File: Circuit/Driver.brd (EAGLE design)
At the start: 160 x 100 mm, 1 part

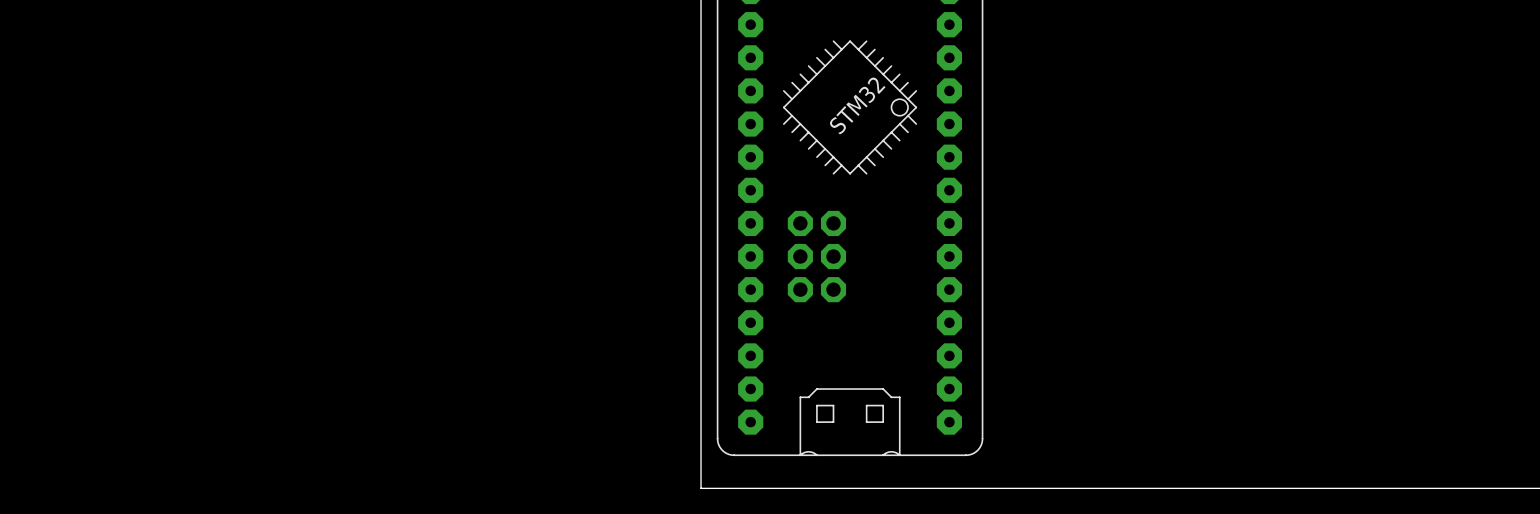
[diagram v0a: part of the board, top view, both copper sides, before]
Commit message: Add the mosfets and their driver to the BLDC Driver sch
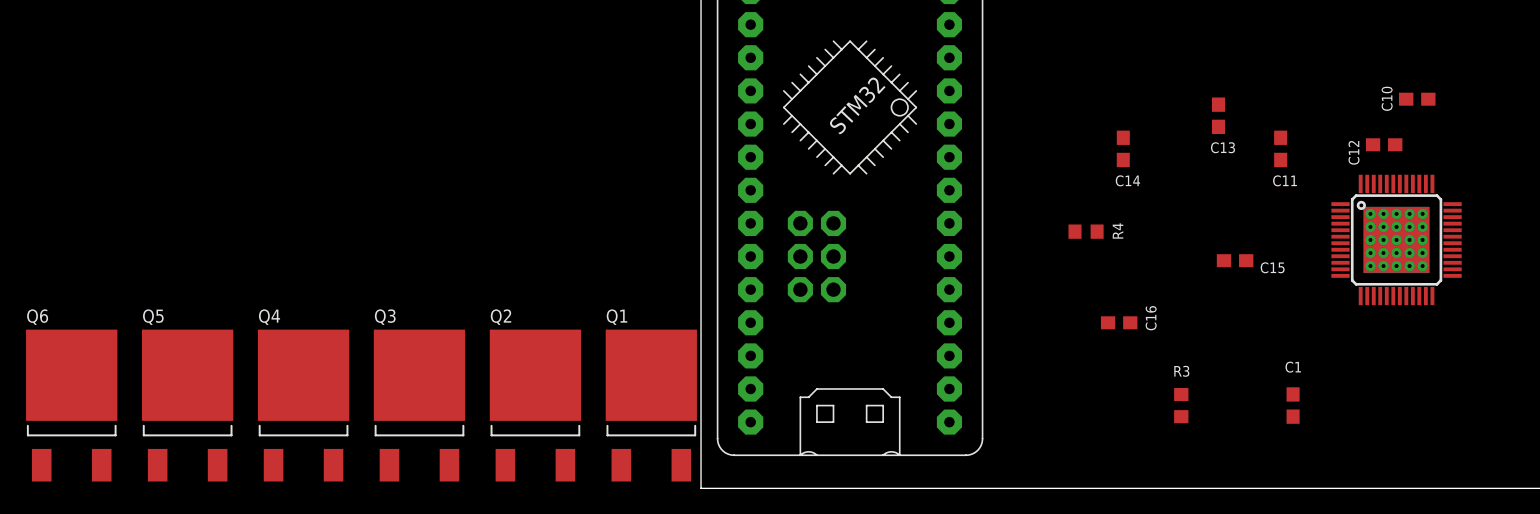
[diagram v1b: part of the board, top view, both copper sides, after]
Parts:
- added C1, C10, C15, C16: 1uF, rcl:C0603
- added C11: 2.2uF, rcl:C0603
- added C12: 4.7uF, rcl:C0603
- added C13, C14: 47nF, rcl:C0603
- added Q1, Q2, Q3, Q4, Q5, Q6: INFINEON_IRLR7843TRPBFINFINEON_IRLR7843TRPBF_0_0, IRLR7843:INFINEON_IRLR7843TRPBF_0
- added R3: 10k, rcl:R0603
- added R4: 100, rcl:R0603
- added U$3: DRV8305, BLDC project:PFB_S-PQFP-G48
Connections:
- net N$20 renamed VIN
- new net +5V: C16.1, R3.1, U$3.48
- new net A3: U$3.16
- new net A4: U$3.17
- new net A5: U$3.18
- new net D1: U$3.1
- new net D14: U$3.4
- new net D15: U$3.6
- new net D16: R3.2, U$3.13
- new net D17: U$3.9
- new net D18: U$3.10
- new net D19: U$3.11
- new net D20: U$3.12
- new net D8: U$3.2
- new net D9: U$3.8
- new net GH_A1: U$3.36
- new net GH_B1: U$3.29
- new net GH_C1: U$3.28
- new net GL_A1: U$3.33
- new net GL_B1: U$3.32
- new net GL_C1: U$3.25
- new net N$1: Q1.3, Q2.4
- new net N$15: C1.1, U$3.15
- new net N$16: C10.1, U$3.37
- new net N$17: C11.2, U$3.38
- new net N$18: C13.2, U$3.40
- new net N$19: C13.1, U$3.39
- new net N$2: Q3.3, Q4.4
- new net N$21: C14.2, U$3.43
- new net N$22: C14.1, U$3.42
- new net N$23: R4.1, U$3.44
- new net N$24: C15.1, U$3.46
- new net N$25: U$3.3
- new net N$26: U$3.5
- new net N$27: U$3.7
- new net N$5: Q5.3, Q6.4
- new net SH_A1: U$3.35
- new net SH_B1: U$3.30
- new net SH_C1: U$3.27
- new net SL_A1: U$3.23, U$3.34
- new net SL_B1: U$3.21, U$3.31
- new net SL_C1: U$3.19, U$3.26
- net GND: now also C1.2, C10.2, C12.2, C15.2, C16.2, U$3.14, U$3.20, U$3.22, U$3.24, U$3.45, U$3.P$1, U$3.P$10, U$3.P$11, U$3.P$12, U$3.P$13, U$3.P$14, U$3.P$15, U$3.P$16, U$3.P$17, U$3.P$18, U$3.P$19, U$3.P$2, U$3.P$20, U$3.P$21, U$3.P$22, U$3.P$23, U$3.P$24, U$3.P$25, U$3.P$26, U$3.P$27, U$3.P$3, U$3.P$4, U$3.P$5, U$3.P$6, U$3.P$7, U$3.P$8, U$3.P$9
- net VCC: now also C11.1, C12.1, R4.2, U$3.41

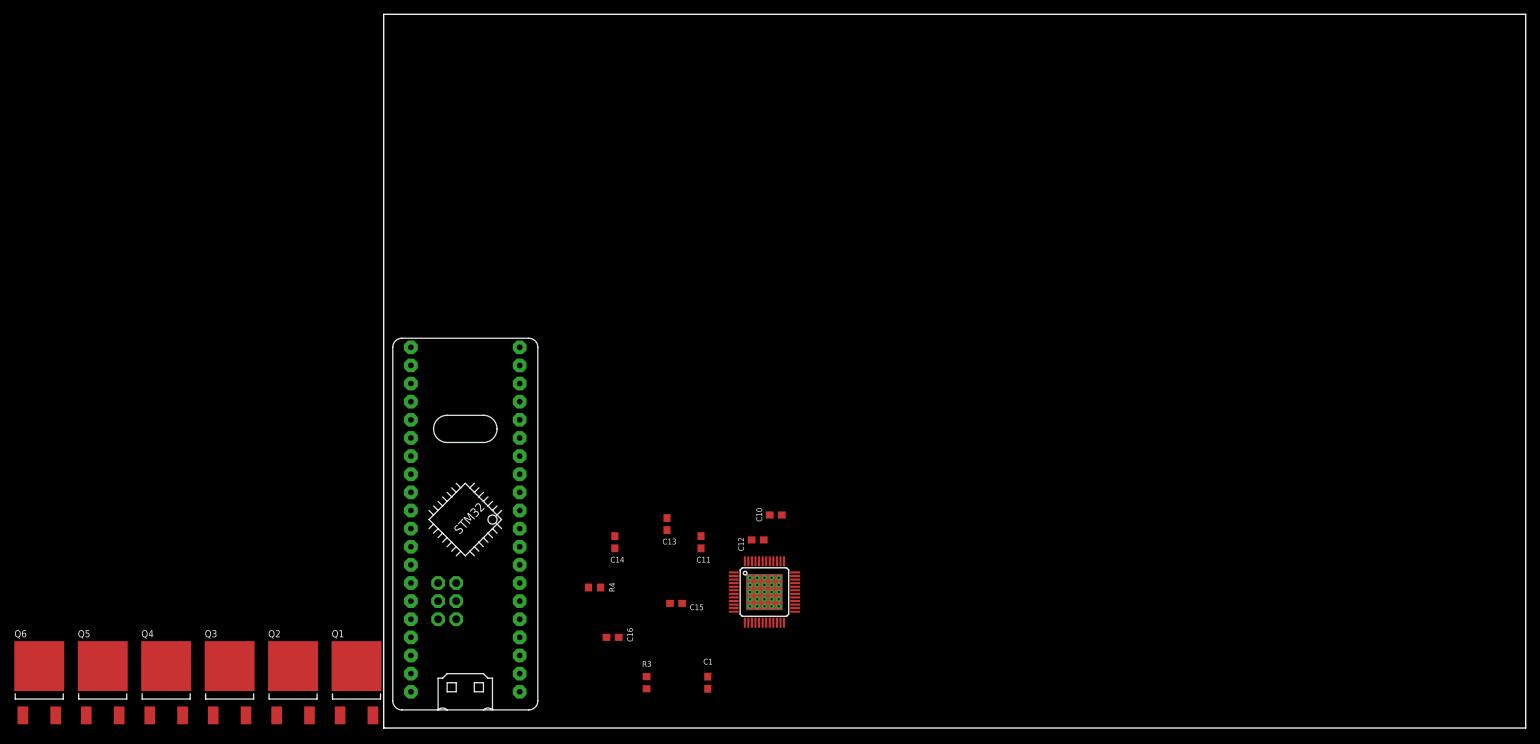
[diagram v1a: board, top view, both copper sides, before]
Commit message: Finish drawing the PCB for 1 stage(not add external layer yet, not autoroutering yet)
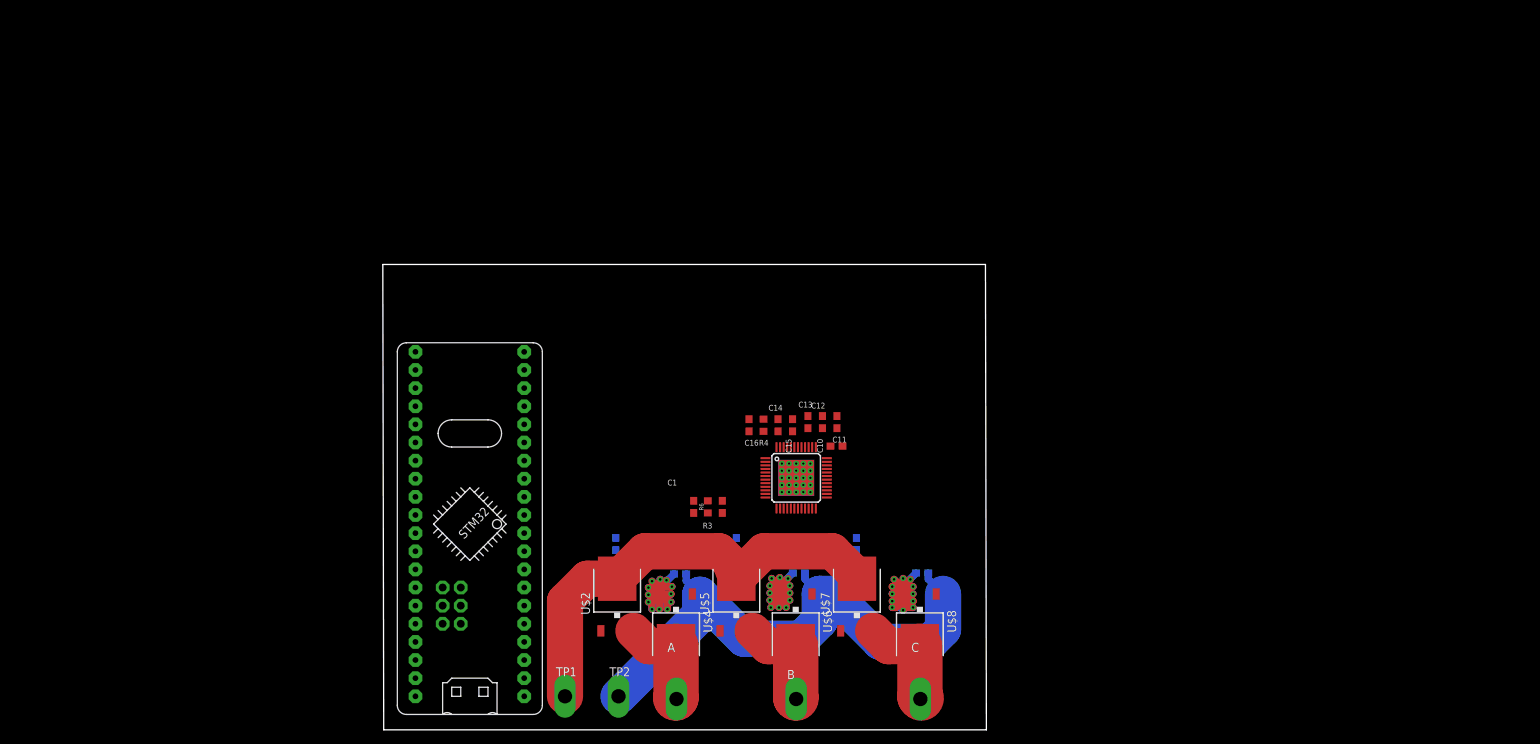
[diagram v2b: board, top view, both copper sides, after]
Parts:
- removed Q1, Q2, Q3, Q4, Q5, Q6: INFINEON_IRLR7843TRPBFINFINEON_IRLR7843TRPBF_0_0, IRLR7843:INFINEON_IRLR7843TRPBF_0
- added A, B, C, TP1, TP2: PTR1PAD1-20Y, testpad:P1-20Y
- added C2, C3, C4: 1nF, SparkFun-Capacitors:0603
- added C5, C6, C7: 1.0uF, SparkFun-Capacitors:0603
- added R1, R2, R5: (no value), rcl:R2512
- added R6: 10k, SparkFun-Resistors:0603
- added U$2, U$4, U$5, U$6, U$7, U$8: IRLR7843, BLDC project:TO252
- moved C16 35.3 mm to (51.2, 42.4), turned to 90 degrees
- moved R4 32.8 mm to (53.2, 42.4), turned to 90 degrees
- moved C15 29.8 mm to (57.3, 42.4), turned to 90 degrees
- moved C14 28.1 mm to (55.2, 42.4), turned to 270 degrees
- moved R3 26.1 mm to (45.4, 31.0), turned to 270 degrees
- moved C11 25.4 mm to (63.5, 42.9)
- moved C1 24.7 mm to (47.4, 31.0), turned to 270 degrees
- moved C13 24.4 mm to (59.4, 42.9), turned to 270 degrees
- moved C12 18.8 mm to (61.5, 42.9), turned to 270 degrees
- moved U$3 16.6 mm to (57.8, 35.1)
- moved C10 12.9 mm to (63.4, 39.5)
- moved U$1 0.90 mm to (9.53, 34.9)
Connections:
- net D16 renamed PWRGD
- net N$16 renamed VCP_LSD
- net N$17 renamed VCPH
- net N$18 renamed CP2L
- net N$19 renamed CP2H
- net N$21 renamed CP1H
- net N$22 renamed CP1L
- net N$23 renamed VDRAIN
- net N$24 renamed DVDD
- removed net +5V: C16.1, R3.1, U$3.48
- removed net A3: U$3.16
- removed net A4: U$3.17
- removed net A5: U$3.18
- removed net D1: U$3.1
- removed net D14: U$3.4
- removed net D15: U$3.6
- removed net D17: U$3.9
- removed net D18: U$3.10
- removed net D19: U$3.11
- removed net D20: U$3.12
- removed net D8: U$3.2
- removed net D9: U$3.8
- removed net GH_A1: U$3.36
- removed net GH_B1: U$3.29
- removed net GH_C1: U$3.28
- removed net GL_A1: U$3.33
- removed net GL_B1: U$3.32
- removed net GL_C1: U$3.25
- removed net N$1: Q1.3, Q2.4
- removed net N$2: Q3.3, Q4.4
- removed net N$25: U$3.3
- removed net N$26: U$3.5
- removed net N$27: U$3.7
- removed net N$5: Q5.3, Q6.4
- removed net SH_A1: U$3.35
- removed net SH_B1: U$3.30
- removed net SH_C1: U$3.27
- removed net SL_A1: U$3.23, U$3.34
- removed net SL_B1: U$3.21, U$3.31
- removed net SL_C1: U$3.19, U$3.26
- new net GH_A: U$2.1, U$3.36
- new net GH_B: U$3.29, U$5.1
- new net GH_C: U$3.28, U$7.1
- new net GL_A: U$3.33, U$4.1
- new net GL_B: U$3.32, U$6.1
- new net GL_C: U$3.25, U$8.1
- new net PVDD: C11.1, C12.1, U$3.41
- new net SH_A: A.TP, U$2.2, U$3.35, U$4.3
- new net SH_B: B.TP, U$3.30, U$5.2, U$6.3
- new net SH_C: C.TP, U$3.27, U$7.2, U$8.3
- new net SN1: C2.2, R1.2, U$3.23, U$3.34, U$4.2
- new net SN2: C3.2, R2.2, U$3.21, U$3.31, U$6.2
- new net SN3: C4.2, R5.2, U$3.19, U$3.26, U$8.2
- new net VIN1: C6.1
- new net VIN2: C7.1
- new net VREG: C16.1, U$3.48
- net GND: now also C2.1, C3.1, C4.1, C5.2, C6.2, C7.2, R1.1, R2.1, R5.1, TP2.TP
- net PA10: now also U$3.4
- net PA3: now also U$3.18
- net PA4: now also U$3.9
- net PA5: now also U$3.12
- net PA6: now also U$3.11
- net PA7: now also U$3.10
- net PA8: now also U$3.2
- net PA9: now also U$3.3
- net PB0: now also U$3.17
- net PB1: now also U$3.16
- net PB12: now also U$3.1
- net PB13: now also R6.2, U$3.8
- net PB6: now also U$3.5
- net PB7: now also U$3.6
- net PB8: now also U$3.7
- net VCC: now also R3.1, R6.1; no longer C11.1, C12.1, R4.2, U$3.41
- net VIN: now also C5.1, R4.2, TP1.TP, U$2.3, U$5.3, U$7.3
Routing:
- net GND: track 0.00 -> 81.1 mm
- net VIN: track 0.00 -> 65.5 mm
- net SN1: track 0.00 -> 56.9 mm, vias 0 -> 12
- net SN3: track 0.00 -> 51.8 mm, vias 0 -> 12
- net SN2: track 0.00 -> 48.4 mm, vias 0 -> 12
- net SH_C: track 0.00 -> 14.8 mm
- net SH_B: track 0.00 -> 14.2 mm
- net SH_A: track 0.00 -> 14.2 mm
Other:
- board size 160 x 100 mm -> 84.6 x 65.2 mm
